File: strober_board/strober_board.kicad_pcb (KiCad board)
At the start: 2 copper layers, 70 x 30 mm, 25 parts, among them J1 Conn_01x02, J2 Conn_01x02, J3 Conn_01x02, J4 AVR-ISP-6, Q1 BC237, Q2 BC237, Q3 BS170, SW1 SW_Push, U1 L78L05_TO92, U2 EL817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

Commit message: changed connectors
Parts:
- moved J1 56.8 mm to (172.7, 73.7), turned to 90 degrees
- moved J3 56.1 mm to (116.8, 66.0), turned to 90 degrees
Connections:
- J1 pad 1: Net-(D1-A) -> Net-(D6-A)
- J1 pad 2: Net-(D3-A) -> Net-(D6-K)
- J3 pad 1: Net-(D6-K) -> Net-(D3-A)
- J3 pad 2: Net-(D6-A) -> Net-(D1-A)
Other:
- board text added: "Adjust or bridge current limiting resistor, depending on connected load!"
- board text removed: "Adjust or bridge current limiting restor, depending on connected load!"

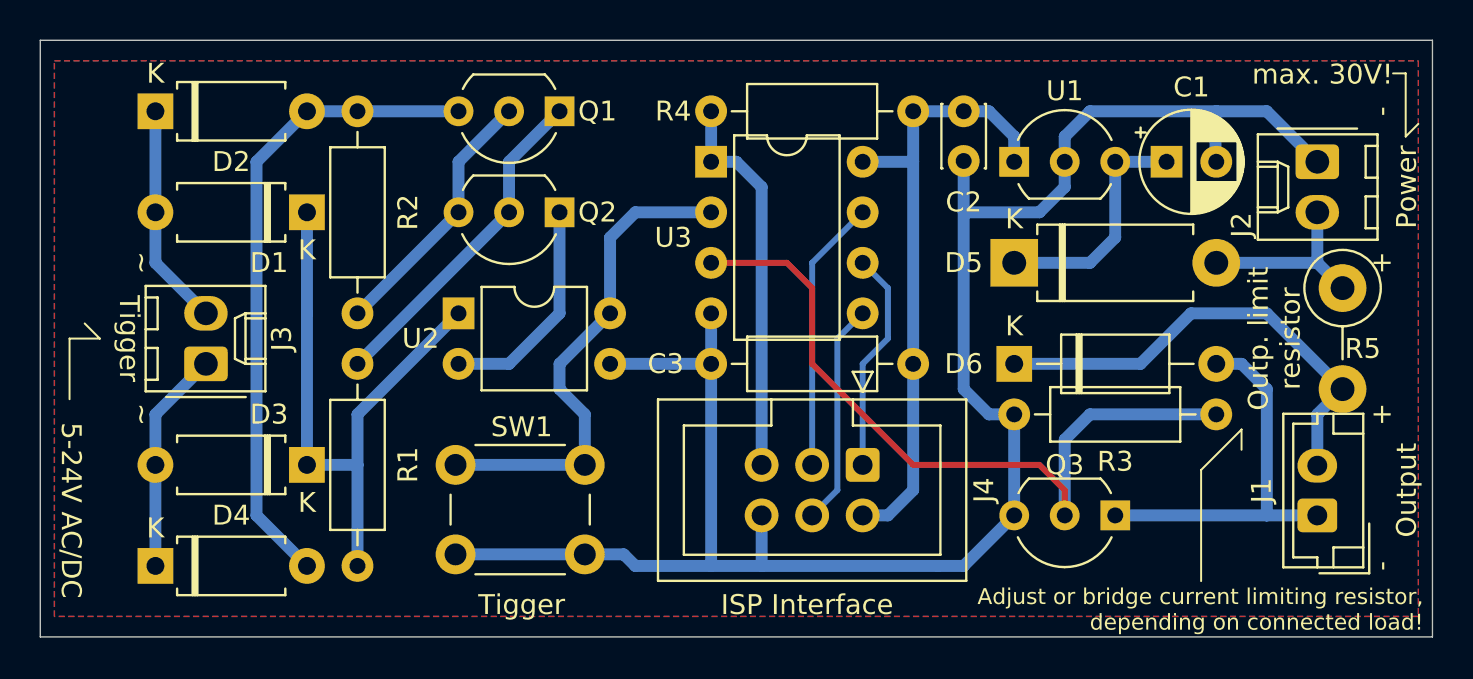
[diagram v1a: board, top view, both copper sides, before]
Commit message: compacted layout
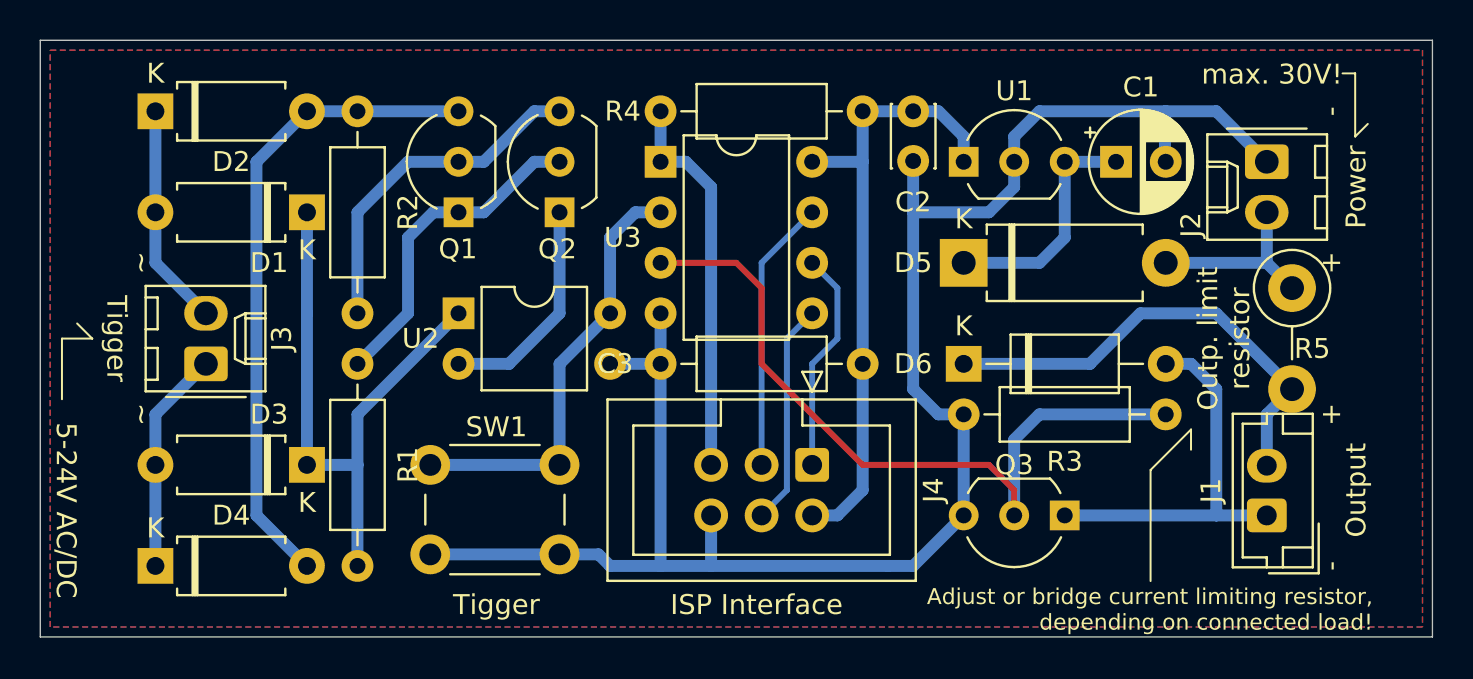
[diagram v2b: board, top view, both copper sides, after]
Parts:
- moved Q1 7.18 mm to (129.5, 58.4), turned to 90 degrees
- moved J4 2.54 mm to (147.3, 71.1)
- moved R5 2.54 mm to (171.4, 62.2)
- moved U3 2.54 mm to (139.7, 55.9)
- moved C1 2.54 mm to (162.6, 55.9)
- moved C2 2.54 mm to (152.4, 55.8)
- moved C3 2.54 mm to (149.9, 66.0)
- moved D5 2.54 mm to (154.9, 61.0)
- moved D6 2.54 mm to (154.9, 66.0)
- moved J1 2.54 mm to (170.2, 73.7)
- moved J2 2.54 mm to (170.2, 55.9)
- moved Q3 2.54 mm to (160.0, 73.7)
- moved R3 2.54 mm to (165.1, 68.6)
- moved R4 2.54 mm to (149.9, 53.3)
- moved U1 2.54 mm to (154.9, 55.9)
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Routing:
- net Net-(Q1-B): track 13.3 -> 17.3 mm
- net GND: track 94.3 -> 90.5 mm
- net /Trigg_{in}: track 25.1 -> 22.0 mm

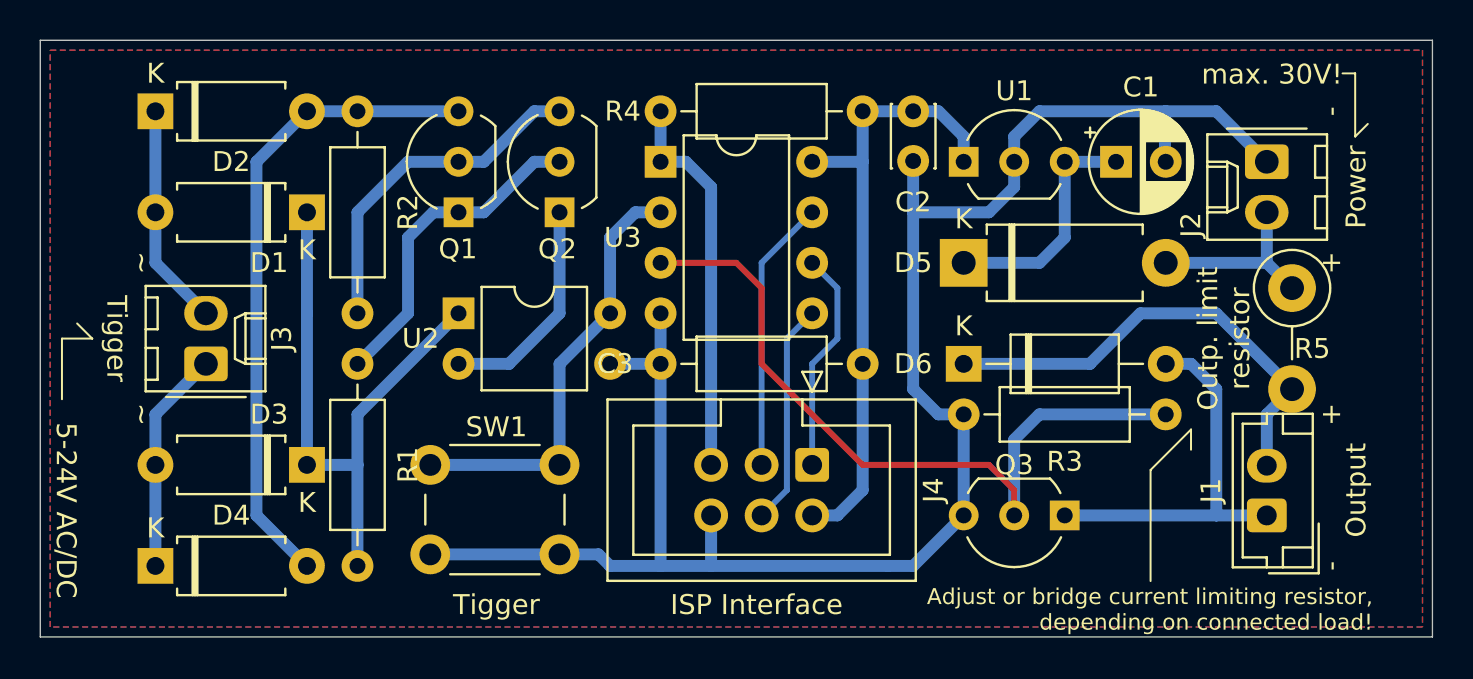
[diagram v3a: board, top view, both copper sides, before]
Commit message: Fixed reverse polarity protection
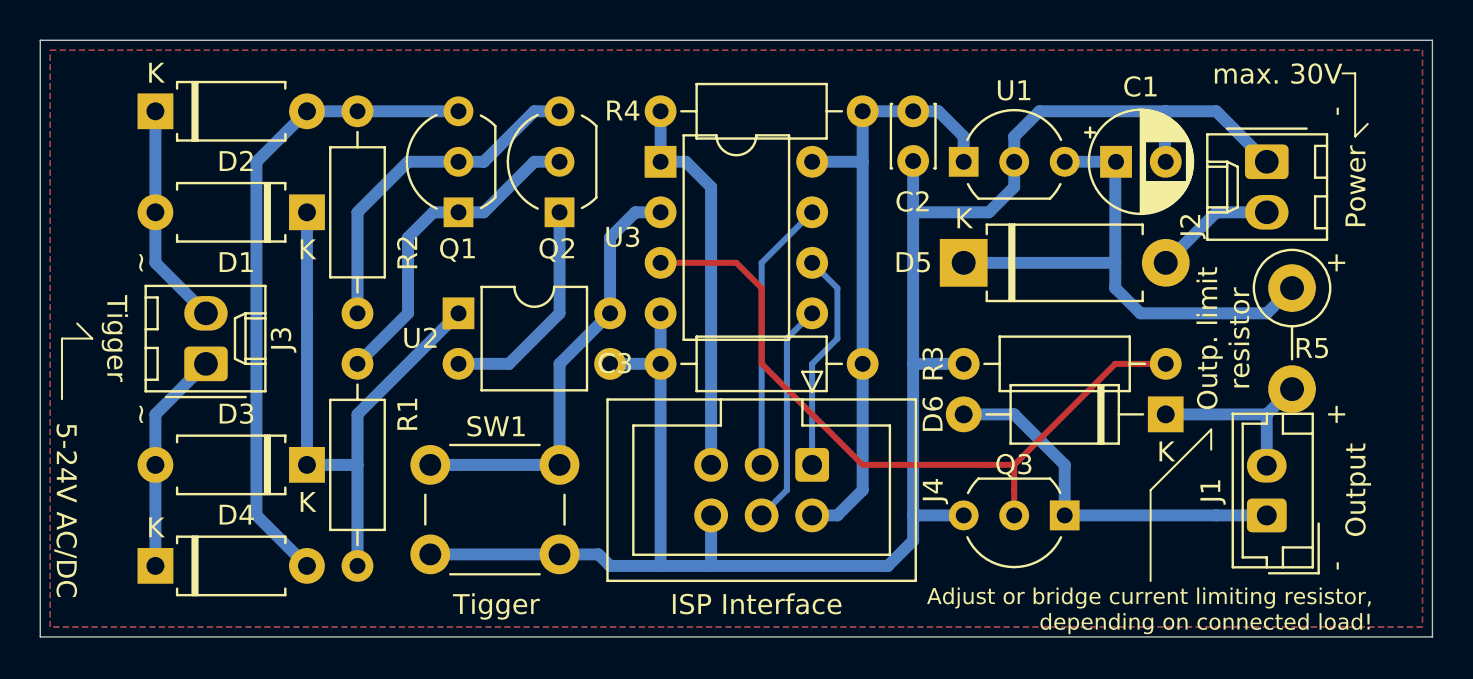
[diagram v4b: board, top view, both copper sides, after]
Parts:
- moved D6 10.5 mm to (165.1, 68.6), turned to 180 degrees
- moved R3 2.54 mm to (165.1, 66.0)
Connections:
- C1 pad 1: Net-(D5-K) -> +12V
- D5 pad 1: Net-(D5-K) -> +12V
- D5 pad 2: +12V -> Net-(D5-A)
- J2 pad 2: +12V -> Net-(D5-A)
- U1 pad 3: Net-(D5-K) -> +12V
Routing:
- net +12V: track 9.42 -> 26.5 mm
- net Net-(D6-K): track 23.5 -> 9.42 mm
- net Net-(D5-K): track 12.0 -> 0.00 mm
- net Net-(D5-A): track 0.00 -> 6.13 mm
- net /LED_{out}: track 38.0 -> 36.5 mm
- net GND: track 90.5 -> 92.0 mm
- net Net-(D6-A): track 19.6 -> 18.8 mm
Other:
- board text added: "max. 30V"
- board text removed: "max. 30V!"

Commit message: fix silkscreen typo
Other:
- board text added: "Trigger"
- board text removed: "Tigger"
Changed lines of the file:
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@@
 		)
 	)
-	(gr_text "Tigger"
+	(gr_text "Trigger"
 		(at 111.76 64.77 270)
 		(layer "F.SilkS" knockout)
@@
 		)
 	)
-	(gr_text "Tigger"
+	(gr_text "Trigger"
 		(at 131.445 78.74 0)
 		(layer "F.SilkS" knockout)
